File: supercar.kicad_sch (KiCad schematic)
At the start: 54 parts, among them SW1 Power, U1 74HC283, U2 74HC574, U3 74HC154, U4 74HC574, U5 74HC86, U6 NE555D

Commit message: Update schematics
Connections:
- net +3.3V is gone; now on net +3V3: RN1.4 (R4.1)
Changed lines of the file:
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@@
   (title_block
     (title "Supercar!")
-    (rev "1")
+    (rev "2")
   )
   (junction (at 24.13 21.59) (diameter 0) (color 0 0 0 0)
@@
     )
   )
+  (symbol (lib_id "power:+3V3") (at 214.63 97.79 0) (unit 1)
+    (in_bom yes) (on_board yes) (dnp no) (fields_autoplaced)
+    (property "Reference" "#PWR030" (at 214.63 101.6 0)
+      (effects (font (size 1.27 1.27)) hide)
+    )
+    (property "Value" "+3V3" (at 214.63 92.71 0)
+      (effects (font (size 1.27 1.27)))
+    )
+    (property "Footprint" "" (at 214.63 97.79 0)
+      (effects (font (size 1.27 1.27)) hide)
+    )
+    (property "Datasheet" "" (at 214.63 97.79 0)
+      (effects (font (size 1.27 1.27)) hide)
+    )
+    (pin "1")
+    (instances
+      (project "supercar"
+        (path "/6cdc46ee-6809-405f-bf74-06040b593f5f"
+          (reference "#PWR030") (unit 1)
+        )
+      )
+    )
+  )
   (symbol (lib_id "Device:LED") (at 243.84 59.69 0) (mirror x) (unit 1)
     (in_bom yes) (on_board yes) (dnp no)
@@
         )
       )
-    )
-  )
-  (symbol (lib_id "power:+3.3V") (at 214.63 97.79 0) (unit 1)
-    (in_bom yes) (on_board yes) (dnp no) (fields_autoplaced)
-    (property "Reference" "#PWR025" (at 214.63 101.6 0)
-      (effects (font (size 1.27 1.27)) hide)
-    )
-    (property "Value" "+3.3V" (at 214.63 92.71 0)
-      (effects (font (size 1.27 1.27)))
-    )
-    (property "Footprint" "" (at 214.63 97.79 0)
-      (effects (font (size 1.27 1.27)) hide)
-    )
-    (property "Datasheet" "" (at 214.63 97.79 0)
-      (effects (font (size 1.27 1.27)) hide)
-    )
-    (pin "1")
-    (instances
-      (project "supercar"
-        (path "/6cdc46ee-6809-405f-bf74-06040b593f5f"
-          (reference "#PWR025") (unit 1)
-        )
-      )

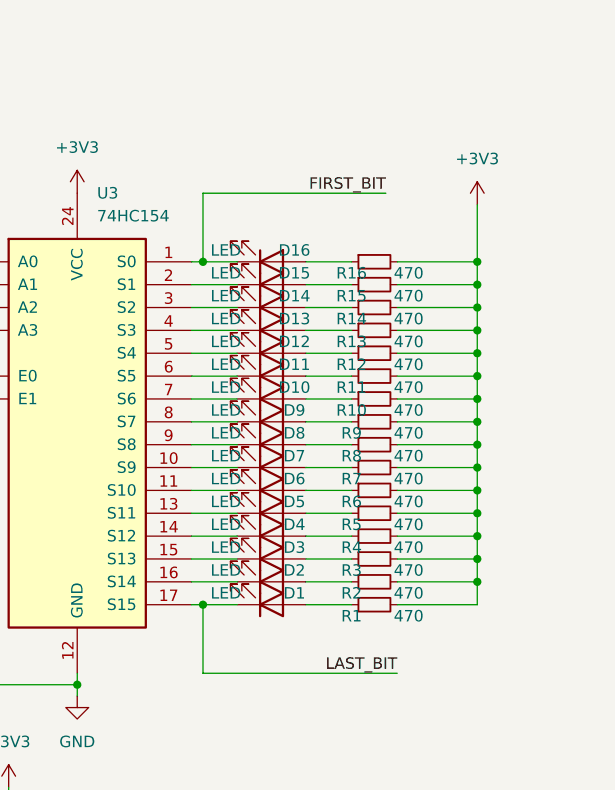
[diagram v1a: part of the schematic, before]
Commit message: Use a single resistor, reduce the size of the PCB
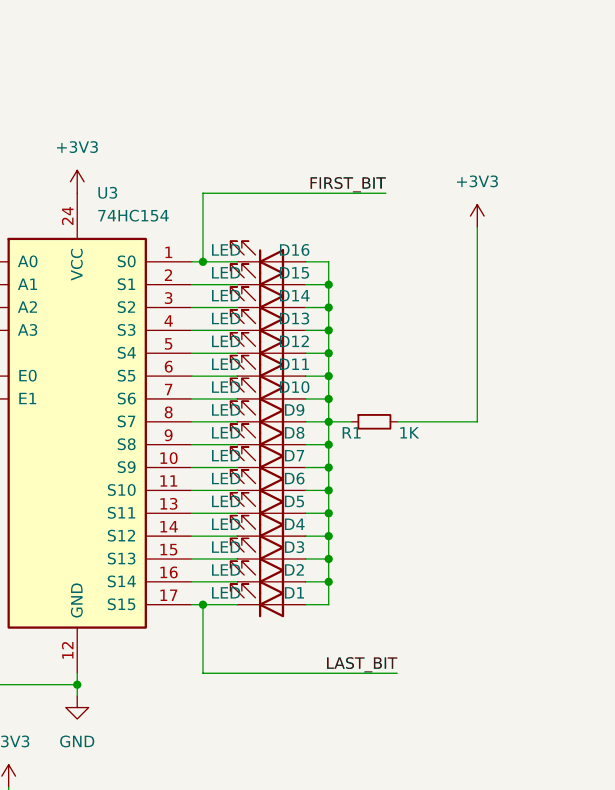
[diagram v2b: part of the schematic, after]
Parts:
- removed R10, R11, R12, R13, R14, R15, R16, R2, R3, R4, R5, R6, R7, R8, R9: 470, Resistor_SMD:R_1206_3216Metric_Pad1.30x1.75mm_HandSolder, symbol Device:R_Small
- R1: value 470 -> 1K
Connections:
- net at D13.2 (A): now also D1.2 (A), D10.2 (A), D11.2 (A), D12.2 (A), D14.2 (A), D15.2 (A), D16.2 (A), D2.2 (A), D3.2 (A), D4.2 (A), D5.2 (A), D6.2 (A), D7.2 (A), D8.2 (A), D9.2 (A), R1.1
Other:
- moved on the sheet: R1

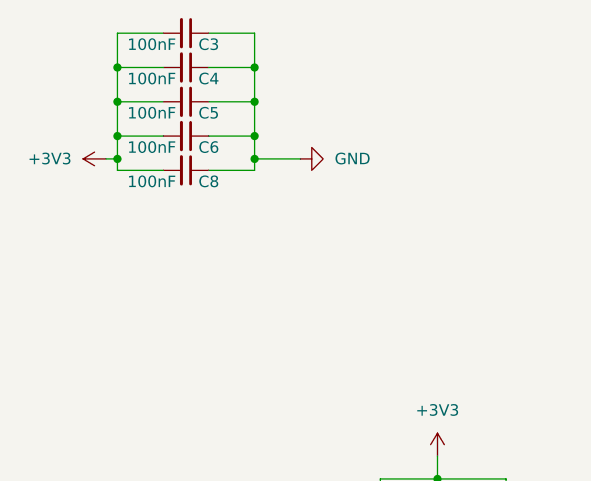
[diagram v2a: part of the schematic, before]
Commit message: Fix cap position in rev3
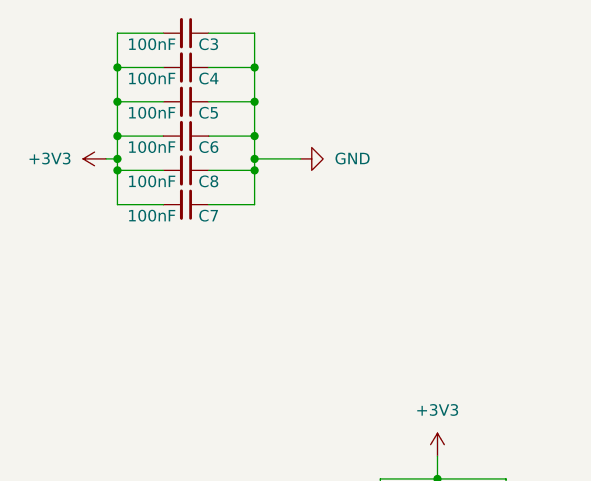
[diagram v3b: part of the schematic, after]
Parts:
- added C7: 100nF, Capacitor_SMD:C_1206_3216Metric_Pad1.33x1.80mm_HandSolder, symbol Device:C_Small
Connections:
- net +3V3: now also C7.2
- net GND: now also C7.1
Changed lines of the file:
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@@
   (junction (at 250.19 72.39) (diameter 0) (color 0 0 0 0)
   )
+  (junction (at 24.13 29.21) (diameter 0) (color 0 0 0 0)
+  )
   (junction (at 250.19 49.53) (diameter 0) (color 0 0 0 0)
   )
   (junction (at 250.19 52.07) (diameter 0) (color 0 0 0 0)
+  )
+  (junction (at 39.37 29.21) (diameter 0) (color 0 0 0 0)
   )
   (junction (at 160.02 52.07) (diameter 0) (color 0 0 0 0)
@@
     (stroke (width 0) (type default))
   )
+  (wire (pts (xy 29.21 33.02) (xy 24.13 33.02))
+    (stroke (width 0) (type default))
+  )
   (wire (pts (xy 158.75 64.77) (xy 158.75 73.66))
     (stroke (width 0) (type default))
@@
     (stroke (width 0) (type default))
   )
+  (wire (pts (xy 24.13 33.02) (xy 24.13 29.21))
+    (stroke (width 0) (type default))
+  )
   (wire (pts (xy 161.29 130.81) (xy 161.29 133.35))
     (stroke (width 0) (type default))
@@
     (stroke (width 0) (type default))
   )
+  (wire (pts (xy 39.37 33.02) (xy 34.29 33.02))
+    (stroke (width 0) (type default))
+  )
   (wire (pts (xy 189.23 39.37) (xy 209.55 39.37))
     (stroke (width 0) (type default))
@@
   )
   (wire (pts (xy 247.65 44.45) (xy 250.19 44.45))
+    (stroke (width 0) (type default))
+  )
+  (wire (pts (xy 39.37 29.21) (xy 39.37 33.02))
     (stroke (width 0) (type default))
   )
@@
         )
       )
+    )
+  )
+  (symbol (lib_id "Device:C_Small") (at 31.75 33.02 270) (unit 1)
+    (in_bom yes) (on_board yes) (dnp no)
+    (property "Reference" "C7" (at 34.29 34.29 90)
+      (effects (font (size 1.27 1.27)))
+    )
+    (property "Value" "100nF" (at 27.94 34.29 90)
+      (effects (font (size 1.27 1.27)))
+    )
+    (property "Footprint" "Capacitor_SMD:C_1206_3216Metric_Pad1.33x1.80mm_HandSolder" (at 31.75 33.02 0)
+      (effects (font (size 1.27 1.27)) hide)
+    )
+    (property "Datasheet" "~" (at 31.75 33.02 0)
+      (effects (font (size 1.27 1.27)) hide)
+    )
+    (pin "2")
+    (pin "1")
+    (instances
+      (project "supercar"
+        (path "/6cdc46ee-6809-405f-bf74-06040b593f5f"
+          (reference "C7") (unit 1)
+        )
+      )

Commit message: Reroute rev_3
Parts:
- RN1: footprint Resistor_SMD:R_Array_Convex_4x1206 -> Resistor_SMD:R_Array_Convex_4x0612
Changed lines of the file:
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@@
       (effects (font (size 1.27 1.27)))
     )
-    (property "Footprint" "Resistor_SMD:R_Array_Convex_4x1206" (at 207.01 95.885 90)
+    (property "Footprint" "Resistor_SMD:R_Array_Convex_4x0612" (at 207.01 95.885 90)
       (effects (font (size 1.27 1.27)) hide)
     )

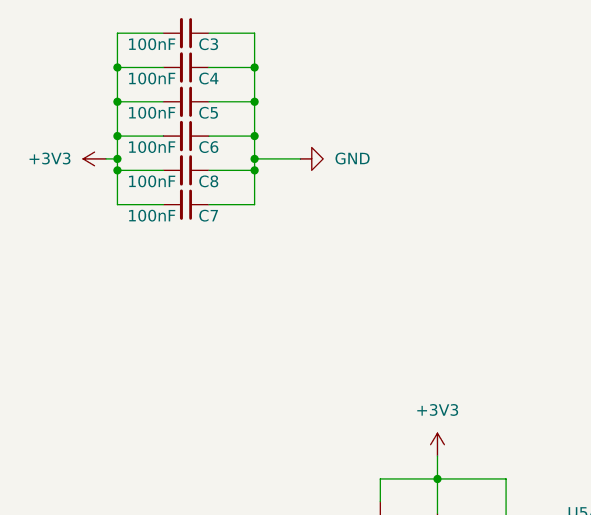
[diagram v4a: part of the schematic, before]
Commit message: add 47uf cap as buffer to battery
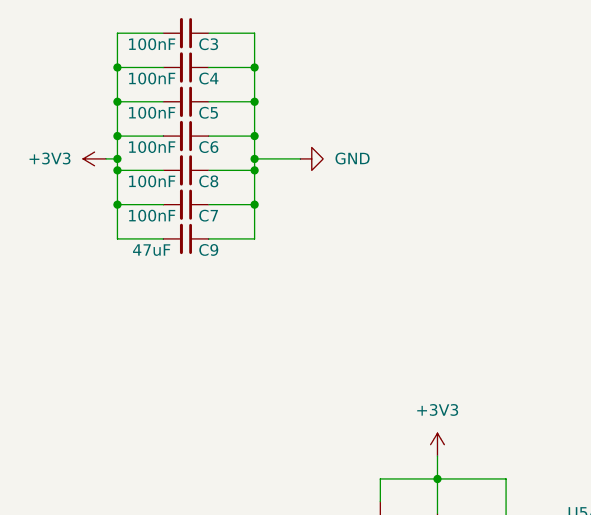
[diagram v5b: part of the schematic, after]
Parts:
- added C9: 47uF, Capacitor_SMD:C_1206_3216Metric_Pad1.33x1.80mm_HandSolder, symbol Device:C_Small
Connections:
- net +3V3: now also C9.2
- net GND: now also C9.1
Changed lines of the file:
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@@
   (junction (at 236.22 39.37) (diameter 0) (color 0 0 0 0)
   )
+  (junction (at 39.37 33.02) (diameter 0) (color 0 0 0 0)
+  )
   (junction (at 176.53 106.68) (diameter 0) (color 0 0 0 0)
   )
@@
   )
   (junction (at 222.25 86.36) (diameter 0) (color 0 0 0 0)
+  )
+  (junction (at 24.13 33.02) (diameter 0) (color 0 0 0 0)
   )
   (junction (at 236.22 77.47) (diameter 0) (color 0 0 0 0)
@@
     (stroke (width 0) (type default))
   )
+  (wire (pts (xy 34.29 36.83) (xy 39.37 36.83))
+    (stroke (width 0) (type default))
+  )
   (wire (pts (xy 256.54 102.87) (xy 266.7 102.87))
     (stroke (width 0) (type default))
@@
     (stroke (width 0) (type default))
   )
+  (wire (pts (xy 29.21 36.83) (xy 24.13 36.83))
+    (stroke (width 0) (type default))
+  )
   (wire (pts (xy 175.26 72.39) (xy 175.26 73.66))
     (stroke (width 0) (type default))
@@
     (stroke (width 0) (type default))
   )
+  (wire (pts (xy 24.13 36.83) (xy 24.13 33.02))
+    (stroke (width 0) (type default))
+  )
   (wire (pts (xy 24.13 25.4) (xy 24.13 27.94))
     (stroke (width 0) (type default))
@@
   )
   (wire (pts (xy 209.55 124.46) (xy 199.39 124.46))
+    (stroke (width 0) (type default))
+  )
+  (wire (pts (xy 39.37 36.83) (xy 39.37 33.02))
     (stroke (width 0) (type default))
   )
@@
         )
       )
+    )
+  )
+  (symbol (lib_id "Device:C_Small") (at 31.75 36.83 270) (unit 1)
+    (in_bom yes) (on_board yes) (dnp no)
+    (property "Reference" "C9" (at 34.29 38.1 90)
+      (effects (font (size 1.27 1.27)))
+    )
+    (property "Value" "47uF" (at 27.94 38.1 90)
+      (effects (font (size 1.27 1.27)))
+    )
+    (property "Footprint" "Capacitor_SMD:C_1206_3216Metric_Pad1.33x1.80mm_HandSolder" (at 31.75 36.83 0)
+      (effects (font (size 1.27 1.27)) hide)
+    )
+    (property "Datasheet" "~" (at 31.75 36.83 0)
+      (effects (font (size 1.27 1.27)) hide)
+    )
+    (pin "2")
+    (pin "1")
+    (instances
+      (project "supercar"
+        (path "/6cdc46ee-6809-405f-bf74-06040b593f5f"
+          (reference "C9") (unit 1)
+        )
+      )

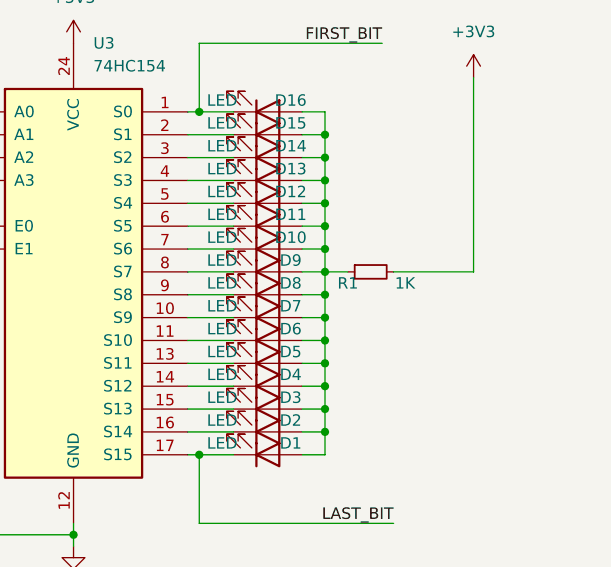
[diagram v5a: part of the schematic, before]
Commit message: Resistor led now 2.2K
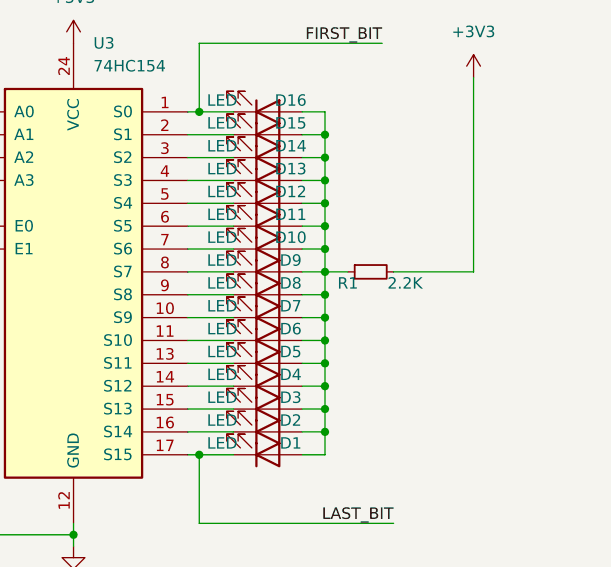
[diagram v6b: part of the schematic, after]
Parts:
- R1: value 1K -> 2.2K
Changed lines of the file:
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@@
       (effects (font (size 1.27 1.27)))
     )
-    (property "Value" "1K" (at 259.08 58.42 90)
+    (property "Value" "2.2K" (at 259.08 58.42 90)
       (effects (font (size 1.27 1.27)))
     )

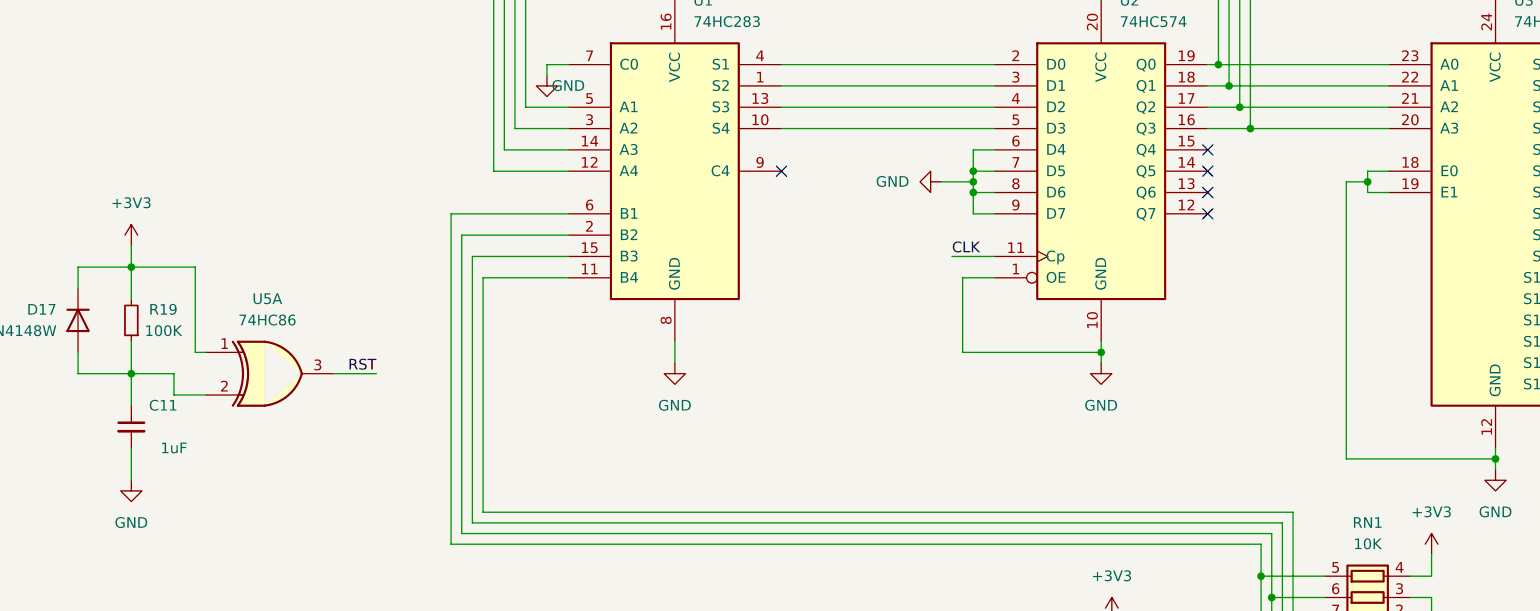
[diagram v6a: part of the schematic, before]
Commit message: Change reset circuit to not turn on leds
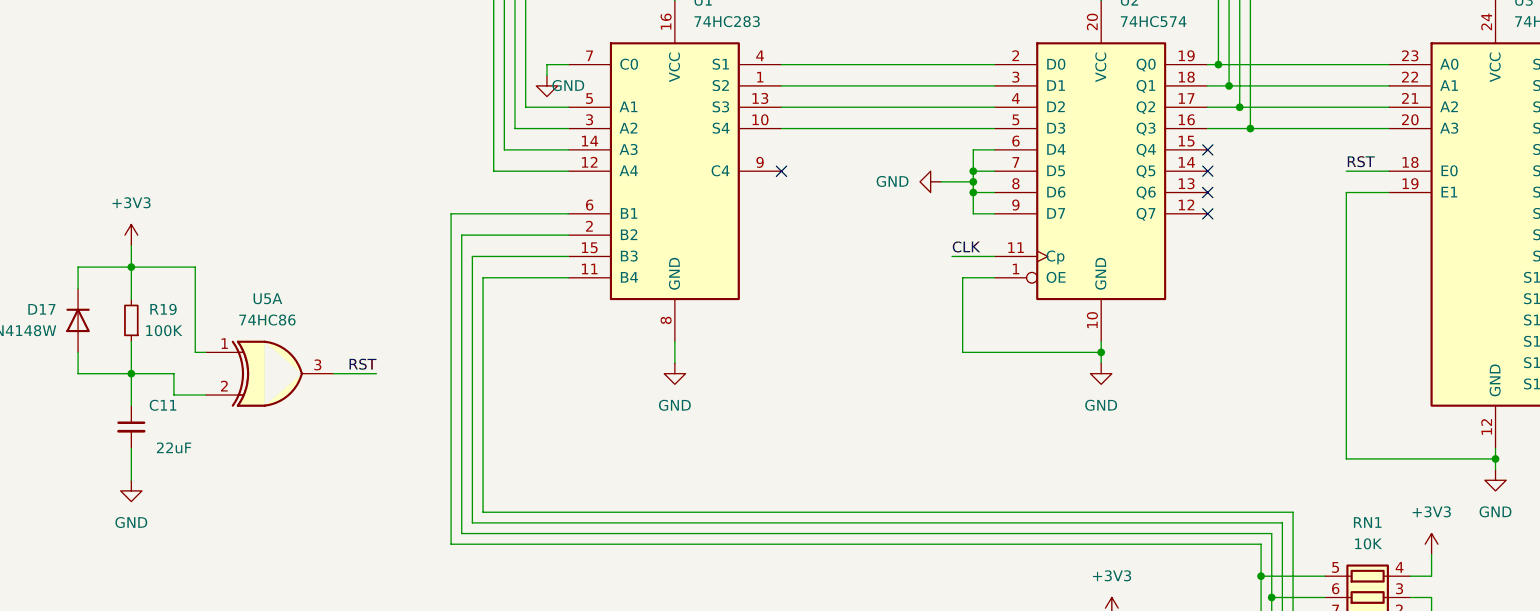
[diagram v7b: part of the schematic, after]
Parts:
- C11: value 1uF -> 22uF
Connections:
- net GND: no longer U3.18 (E0)
- net RST: now also U3.18 (E0)
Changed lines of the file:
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@@
   (junction (at 273.05 129.54) (diameter 0) (color 0 0 0 0)
-  )
-  (junction (at 207.01 53.34) (diameter 0) (color 0 0 0 0)
   )
   (junction (at 250.19 59.69) (diameter 0) (color 0 0 0 0)
@@
     (stroke (width 0) (type default))
   )
-  (wire (pts (xy 204.47 53.34) (xy 204.47 86.36))
-    (stroke (width 0) (type default))
-  )
   (wire (pts (xy 234.95 74.93) (xy 240.03 74.93))
     (stroke (width 0) (type default))
@@
     (stroke (width 0) (type default))
   )
-  (wire (pts (xy 207.01 52.07) (xy 207.01 53.34))
-    (stroke (width 0) (type default))
-  )
   (wire (pts (xy 104.14 140.97) (xy 107.95 140.97))
     (stroke (width 0) (type default))
@@
     (stroke (width 0) (type default))
   )
+  (wire (pts (xy 204.47 54.61) (xy 204.47 86.36))
+    (stroke (width 0) (type default))
+  )
   (wire (pts (xy 234.95 69.85) (xy 240.03 69.85))
     (stroke (width 0) (type default))
@@
     (stroke (width 0) (type default))
   )
-  (wire (pts (xy 207.01 53.34) (xy 204.47 53.34))
-    (stroke (width 0) (type default))
-  )
   (wire (pts (xy 198.12 107.95) (xy 201.93 107.95))
     (stroke (width 0) (type default))
@@
     (stroke (width 0) (type default))
   )
-  (wire (pts (xy 207.01 53.34) (xy 207.01 54.61))
-    (stroke (width 0) (type default))
-  )
   (wire (pts (xy 158.75 118.11) (xy 158.75 120.65))
     (stroke (width 0) (type default))
@@
     (stroke (width 0) (type default))
   )
-  (wire (pts (xy 207.01 54.61) (xy 209.55 54.61))
+  (wire (pts (xy 204.47 54.61) (xy 209.55 54.61))
     (stroke (width 0) (type default))
   )
@@
     (stroke (width 0) (type default))
   )
-  (wire (pts (xy 209.55 52.07) (xy 207.01 52.07))
+  (wire (pts (xy 204.47 52.07) (xy 209.55 52.07))
     (stroke (width 0) (type default))
   )
@@
   (label "RST" (at 170.18 149.86 180) (fields_autoplaced)
     (effects (font (size 1.27 1.27)) (justify right bottom))
+  )
+  (label "RST" (at 204.47 52.07 0) (fields_autoplaced)
+    (effects (font (size 1.27 1.27)) (justify left bottom))
   )
   (label "FIRST_BIT" (at 256.54 31.75 180) (fields_autoplaced)
@@
       (effects (font (size 1.27 1.27)))
     )
-    (property "Value" "1uF" (at 64.77 85.09 0)
-      (effects (font (size 1.27 1.27)))
-    )
+    (property "Value" "22uF" (at 64.77 85.09 0)
+      (effects (font (size 1.27 1.27)))
+    )

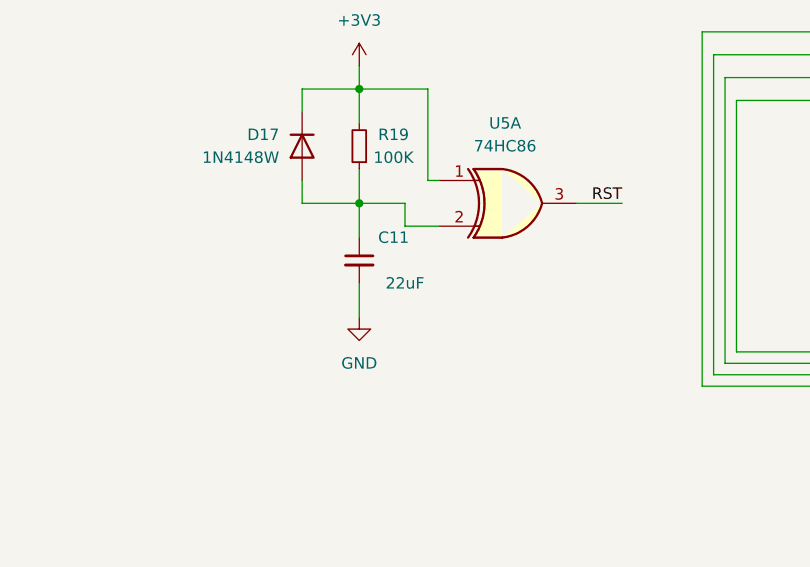
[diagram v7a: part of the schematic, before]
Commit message: Small change in component value
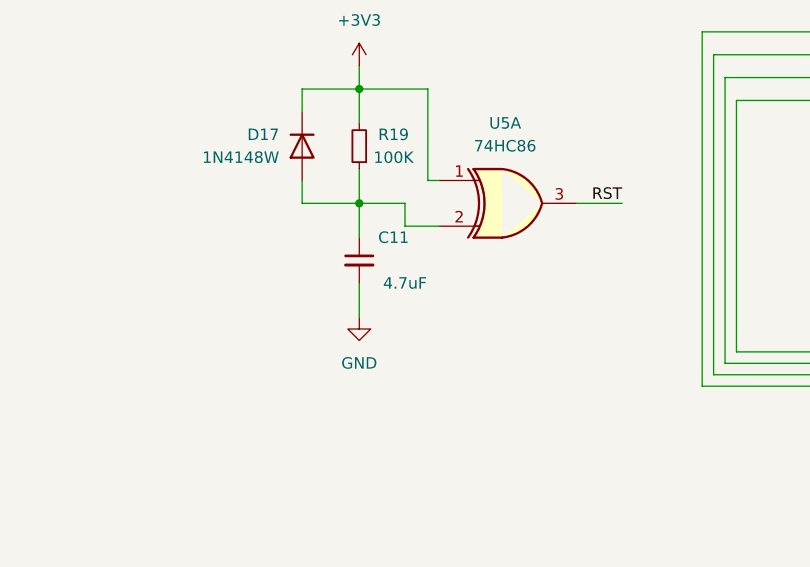
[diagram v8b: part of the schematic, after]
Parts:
- C11: value 22uF -> 4.7uF
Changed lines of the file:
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@@
       (effects (font (size 1.27 1.27)))
     )
-    (property "Value" "22uF" (at 64.77 85.09 0)
+    (property "Value" "4.7uF" (at 64.77 85.09 0)
       (effects (font (size 1.27 1.27)))
     )
